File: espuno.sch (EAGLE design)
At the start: 62 parts, among them J1 ARDUINO_R3_SHIELD, T1 FDN340P, U1 ADS1115IDGST, U2 NCP1117ST50T3G, U3 LP2985-33DBVR, U4 FT232R, U5 LMV358IDGKR, U6 MCP73831, U7 TPS61200, X1 POWERSUPPLY_DC21MMX

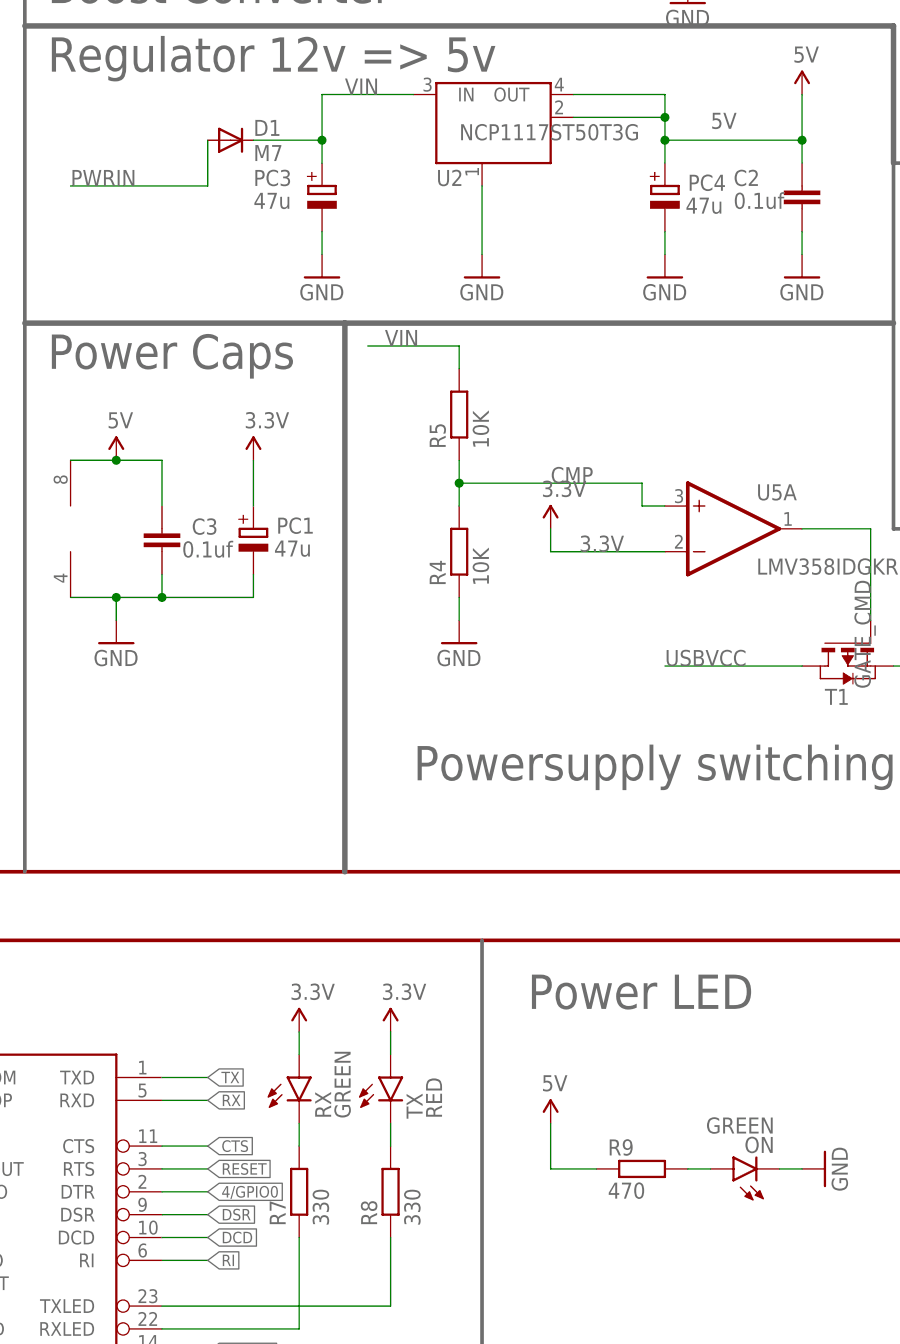
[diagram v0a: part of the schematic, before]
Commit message: Fix bug with TX/RX switched, renumber PC1,PC3,PC4 to be PC1-3 in order of decreasing voltage rail.
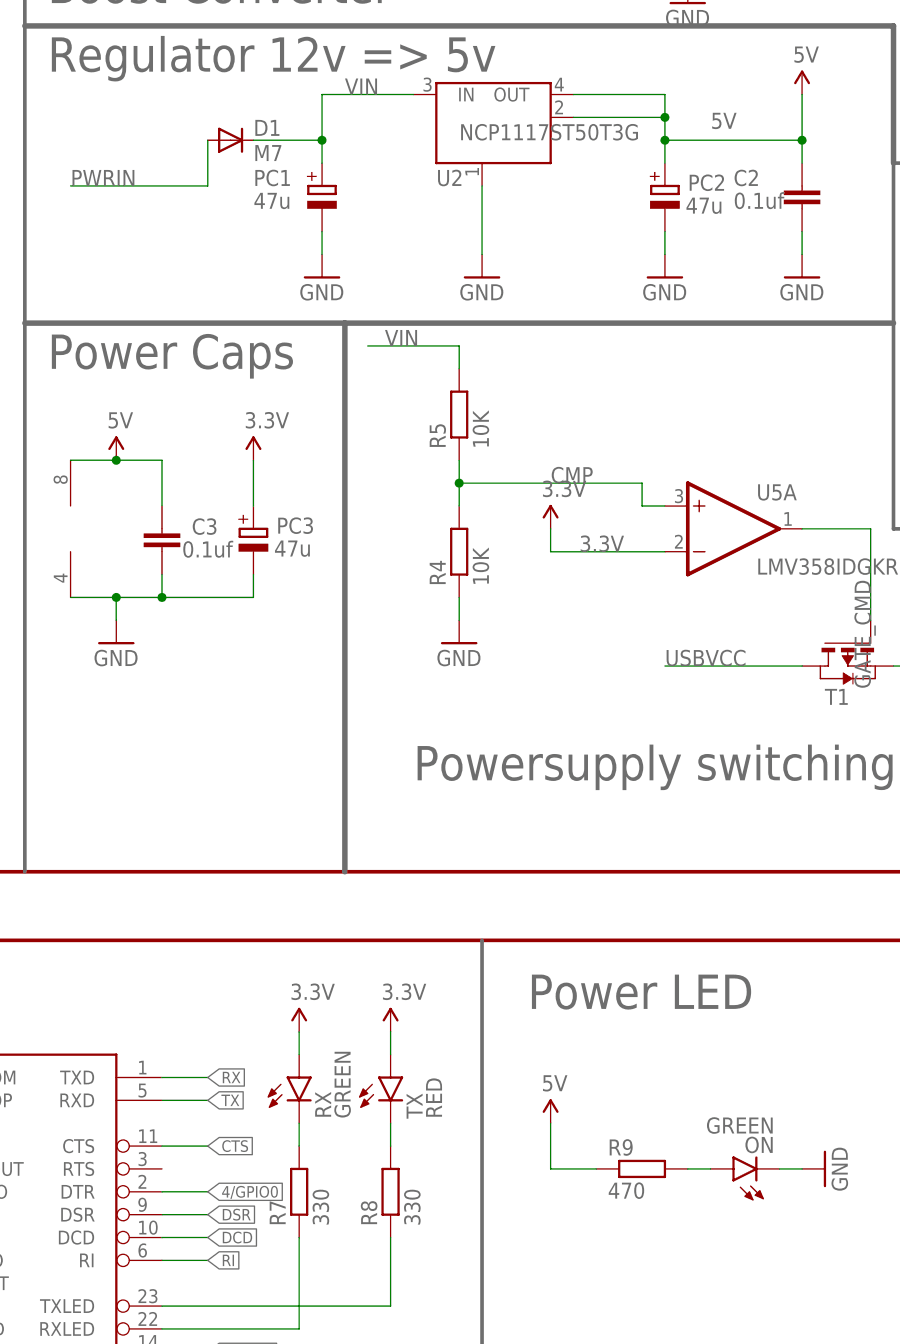
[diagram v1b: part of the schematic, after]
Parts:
- renumbered PC4 to PC2
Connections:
- net 3.3V: now also PC3.+; no longer PC1.+
- net RESET: no longer U4.RTS
- net RX: now also U4.TXD; no longer U4.RXD
- net TX: now also U4.RXD; no longer U4.TXD
- net VIN: now also PC1.+; no longer PC3.+
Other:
- moved on the sheet: PC1, PC3
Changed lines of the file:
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@@
 <?xml version="1.0" encoding="utf-8"?>
 <!DOCTYPE eagle SYSTEM "eagle.dtd">
-<eagle version="7.2.0">
+<eagle version="7.4.0">
 <drawing>
 <settings>
@@
 <part name="JP1" library="SparkFun-Connectors" deviceset="USB" device="-SMD-NS"/>
 <part name="J1" library="SparkFun-Boards" deviceset="ARDUINO_R3_SHIELD" device=""/>
+<part name="PC1" library="rcl" deviceset="CPOL-EU" device="D" value="47u"/>
+<part name="PC2" library="rcl" deviceset="CPOL-EU" device="D" value="47u"/>
 <part name="PC3" library="rcl" deviceset="CPOL-EU" device="D" value="47u"/>
-<part name="PC4" library="rcl" deviceset="CPOL-EU" device="D" value="47u"/>
-<part name="PC1" library="rcl" deviceset="CPOL-EU" device="D" value="47u"/>
 <part name="SUPPLY15" library="SparkFun-Aesthetics" deviceset="3.3V" device=""/>
 <part name="FLASH" library="switch-omron" deviceset="10-XX" device=""/>
@@
 <instance part="JP1" gate="G$1" x="22.86" y="233.68" rot="MR0"/>
 <instance part="J1" gate="G$1" x="40.64" y="287.02"/>
-<instance part="PC3" gate="G$1" x="119.38" y="269.24" smashed="yes">
+<instance part="PC1" gate="G$1" x="119.38" y="269.24" smashed="yes">
 <attribute name="NAME" x="111.76" y="269.24" size="1.778" layer="95"/>
 <attribute name="VALUE" x="111.76" y="266.7" size="1.778" layer="96"/>
 </instance>
-<instance part="PC4" gate="G$1" x="157.48" y="269.24" smashed="yes">
+<instance part="PC2" gate="G$1" x="157.48" y="269.24" smashed="yes">
 <attribute name="NAME" x="160.02" y="268.7066" size="1.778" layer="95"/>
 <attribute name="VALUE" x="159.766" y="266.1666" size="1.778" layer="96"/>
 </instance>
-<instance part="PC1" gate="G$1" x="111.76" y="231.14" smashed="yes">
+<instance part="PC3" gate="G$1" x="111.76" y="231.14" smashed="yes">
 <attribute name="NAME" x="114.3" y="230.6066" size="1.778" layer="95"/>
 <attribute name="VALUE" x="114.046" y="228.0666" size="1.778" layer="96"/>
@@
 <label x="226.06" y="167.64" size="1.778" layer="95"/>
 </segment>
-<segment>
-<wire x1="101.6" y1="160.02" x2="106.68" y2="160.02" width="0.1524" layer="91"/>
-<pinref part="U4" gate="G$1" pin="RTS"/>
-<label x="106.68" y="160.02" size="1.27" layer="95" xref="yes"/>
-</segment>
 </net>
 <net name="3.3V" class="0">
@@
 <segment>
 <pinref part="SUPPLY15" gate="G$1" pin="3.3V"/>
-<pinref part="PC1" gate="G$1" pin="+"/>
+<pinref part="PC3" gate="G$1" pin="+"/>
 <wire x1="111.76" y1="238.76" x2="111.76" y2="233.68" width="0.1524" layer="91"/>
 </segment>
@@
 <wire x1="157.48" y1="264.16" x2="157.48" y2="261.62" width="0.1524" layer="91"/>
 <pinref part="GND10" gate="1" pin="GND"/>
-<pinref part="PC4" gate="G$1" pin="-"/>
+<pinref part="PC2" gate="G$1" pin="-"/>
 </segment>
 <segment>
 <wire x1="119.38" y1="261.62" x2="119.38" y2="264.16" width="0.1524" layer="91"/>
 <pinref part="GND9" gate="1" pin="GND"/>
-<pinref part="PC3" gate="G$1" pin="-"/>
+<pinref part="PC1" gate="G$1" pin="-"/>
 </segment>
 <segment>
@@
 <pinref part="U5" gate="P" pin="V-"/>
 <wire x1="111.76" y1="226.06" x2="111.76" y2="223.52" width="0.1524" layer="91"/>
-<pinref part="PC1" gate="G$1" pin="-"/>
+<pinref part="PC3" gate="G$1" pin="-"/>
 <wire x1="111.76" y1="223.52" x2="101.6" y2="223.52" width="0.1524" layer="91"/>
 <junction x="101.6" y="223.52"/>
@@
 </segment>
 <segment>
+<wire x1="53.34" y1="304.8" x2="66.04" y2="304.8" width="0.1524" layer="91"/>
+<pinref part="J1" gate="G$1" pin="RX"/>
+<label x="55.88" y="304.8" size="1.778" layer="95"/>
+</segment>
+<segment>
+<wire x1="101.6" y1="170.18" x2="106.68" y2="170.18" width="0.1524" layer="91"/>
+<pinref part="U4" gate="G$1" pin="TXD"/>
+<label x="106.68" y="170.18" size="1.27" layer="95" xref="yes"/>
+</segment>
+</net>
+<net name="TX" class="0">
+<segment>
+<wire x1="76.2" y1="360.68" x2="55.88" y2="360.68" width="0.1524" layer="91"/>
+<label x="63.5" y="360.68" size="1.778" layer="95"/>
+<pinref part="MDL1" gate="G$1" pin="TXD"/>
+</segment>
+<segment>
+<pinref part="J1" gate="G$1" pin="TX"/>
+<wire x1="53.34" y1="302.26" x2="66.04" y2="302.26" width="0.1524" layer="91"/>
+<label x="55.88" y="302.26" size="1.778" layer="95"/>
+</segment>
+<segment>
 <wire x1="101.6" y1="167.64" x2="106.68" y2="167.64" width="0.1524" layer="91"/>
 <pinref part="U4" gate="G$1" pin="RXD"/>
 <label x="106.68" y="167.64" size="1.27" layer="95" xref="yes"/>
-</segment>
-<segment>
-<wire x1="53.34" y1="304.8" x2="66.04" y2="304.8" width="0.1524" layer="91"/>
-<pinref part="J1" gate="G$1" pin="RX"/>
-<label x="55.88" y="304.8" size="1.778" layer="95"/>
-</segment>
-</net>
-<net name="TX" class="0">
-<segment>
-<wire x1="76.2" y1="360.68" x2="55.88" y2="360.68" width="0.1524" layer="91"/>
-<label x="63.5" y="360.68" size="1.778" layer="95"/>
-<pinref part="MDL1" gate="G$1" pin="TXD"/>
-</segment>
-<segment>
-<wire x1="101.6" y1="170.18" x2="106.68" y2="170.18" width="0.1524" layer="91"/>
-<pinref part="U4" gate="G$1" pin="TXD"/>
-<label x="106.68" y="170.18" size="1.27" layer="95" xref="yes"/>
-</segment>
-<segment>
-<pinref part="J1" gate="G$1" pin="TX"/>
-<wire x1="53.34" y1="302.26" x2="66.04" y2="302.26" width="0.1524" layer="91"/>
-<label x="55.88" y="302.26" size="1.778" layer="95"/>
 </segment>
 </net>
@@
 <pinref part="C2" gate="G$1" pin="2"/>
 <junction x="172.72" y="274.32"/>
-<pinref part="PC4" gate="G$1" pin="+"/>
+<pinref part="PC2" gate="G$1" pin="+"/>
 </segment>
 <segment>
@@
 <pinref part="U2" gate="G$1" pin="IN"/>
 <pinref part="D1" gate="G$1" pin="C"/>
-<pinref part="PC3" gate="G$1" pin="+"/>
-</segment>
-<segment>
+<pinref part="PC1" gate="G$1" pin="+"/>
+</segment>
+<segment>

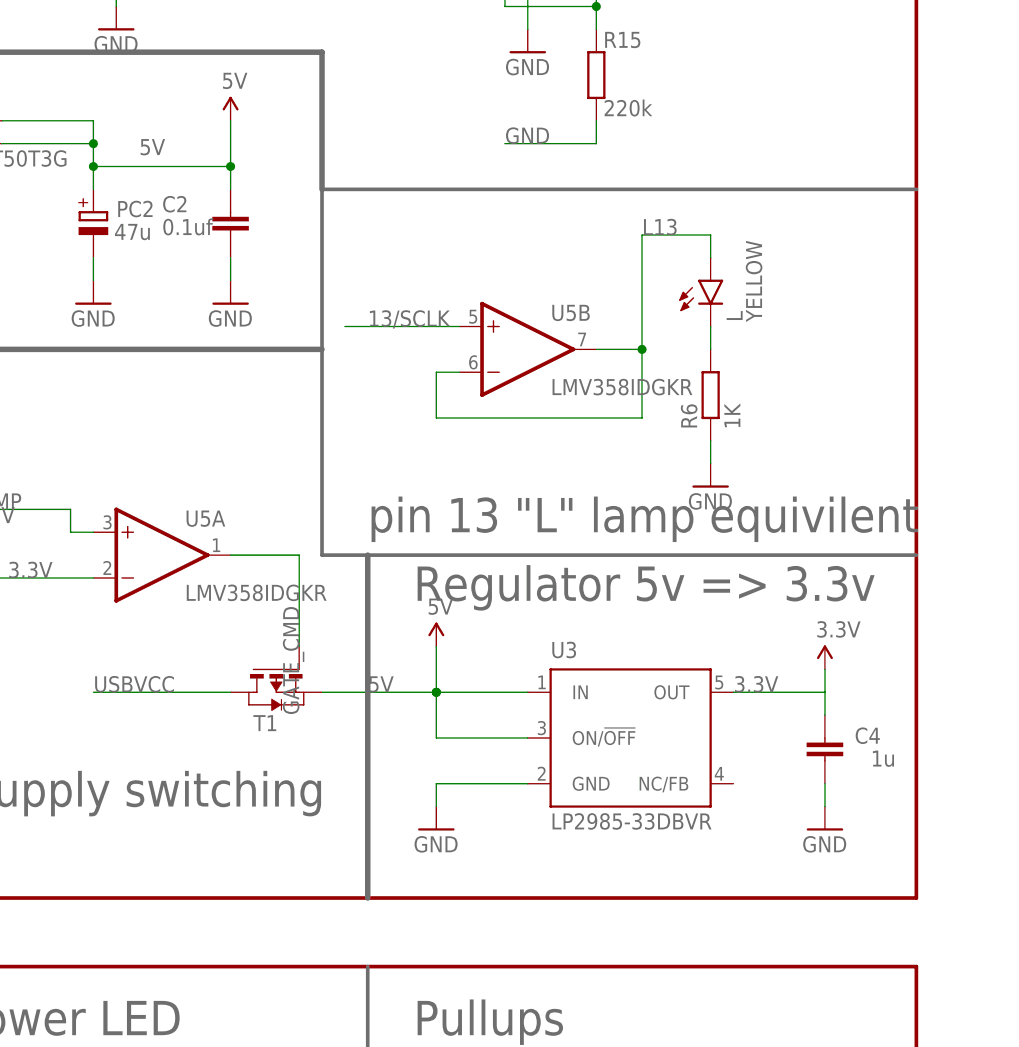
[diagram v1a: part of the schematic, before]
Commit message: Change puny 3.3v regulator for a 800mA-1A regulator. Rearrangements to make space, remove redundent capacitor
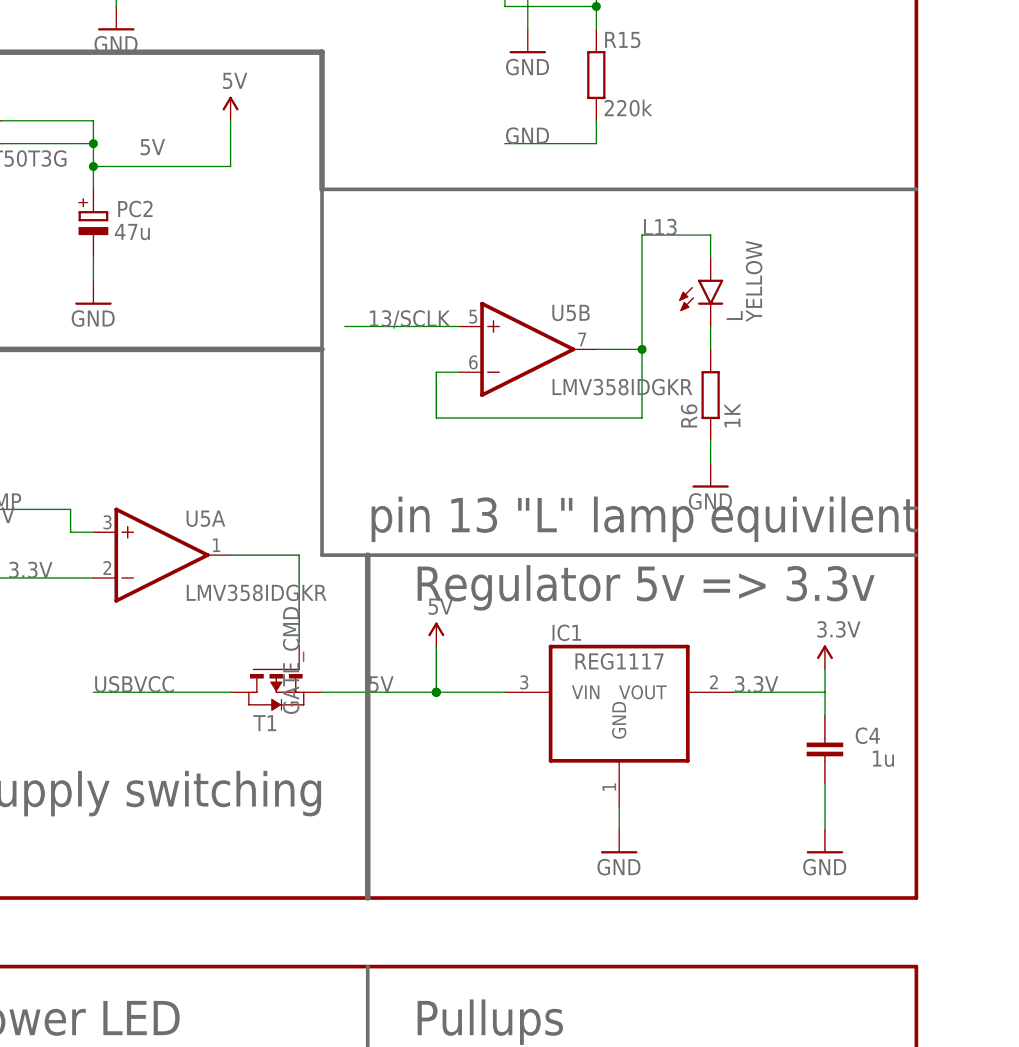
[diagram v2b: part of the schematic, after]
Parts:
- removed C2: 0.1uf, rcl:C-EUC1206K
- removed U3: LP2985-33DBVR, SmartPrj:LP2985-XXDBVR33
- added IC1: REG1117, burr-brown:REG1117
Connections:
- net 3.3V: now also IC1.VOUT; no longer U3.OUT
- net 5V: now also IC1.VIN; no longer C2.2, U3.IN, U3.ON/!OFF
- net GND: now also IC1.GND; no longer C2.1, U3.GND
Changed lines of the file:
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@@
 <part name="R3" library="rcl" deviceset="R-EU_" device="M1206" value="10K"/>
 <part name="U$6" library="microbuilder" deviceset="GND" device=""/>
-<part name="C2" library="rcl" deviceset="C-EU" device="C1206K" value="0.1uf"/>
-<part name="GND7" library="supply1" deviceset="GND" device=""/>
 <part name="GND9" library="supply1" deviceset="GND" device=""/>
 <part name="GND10" library="supply1" deviceset="GND" device=""/>
@@
 <part name="C4" library="rcl" deviceset="C-EU" device="C1206K" value="1u"/>
 <part name="U5" library="linear" deviceset="LMV358?*" device="MM" technology="X" value="LMV358IDGKR"/>
-<part name="U3" library="SmartPrj" deviceset="LP2985-XXDBVR" device="" technology="33" value="LP2985-33DBVR"/>
 <part name="R4" library="rcl" deviceset="R-EU_" device="M1206" value="10K"/>
 <part name="R5" library="rcl" deviceset="R-EU_" device="M1206" value="10K"/>
@@
 <part name="R20" library="SparkFun-Resistors" deviceset="RESISTOR" device="1206" value="10k"/>
 <part name="R21" library="SparkFun-Resistors" deviceset="RESISTOR" device="1206" value="10k"/>
+<part name="IC1" library="burr-brown" deviceset="REG1117" device=""/>
 </parts>
 <sheets>
@@
 <instance part="R3" gate="G$1" x="73.66" y="68.58" rot="R270"/>
 <instance part="U$6" gate="G$1" x="73.66" y="58.42"/>
-<instance part="C2" gate="G$1" x="172.72" y="266.7" smashed="yes" rot="R180">
-<attribute name="NAME" x="165.1" y="269.24" size="1.778" layer="95"/>
-<attribute name="VALUE" x="165.1" y="266.7" size="1.778" layer="96"/>
-</instance>
-<instance part="GND7" gate="1" x="172.72" y="259.08"/>
 <instance part="GND9" gate="1" x="119.38" y="259.08"/>
 <instance part="GND10" gate="1" x="157.48" y="259.08"/>
@@
 <attribute name="VALUE" x="109.474" y="227.965" size="1.778" layer="96" rot="MR0"/>
 </instance>
-<instance part="GND21" gate="1" x="238.76" y="200.66"/>
-<instance part="GND4" gate="1" x="195.58" y="200.66"/>
+<instance part="GND21" gate="1" x="238.76" y="198.12"/>
+<instance part="GND4" gate="1" x="215.9" y="198.12"/>
 <instance part="C4" gate="G$1" x="238.76" y="208.28" smashed="yes" rot="MR180">
 <attribute name="NAME" x="244.983" y="210.185" size="1.778" layer="95" rot="MR0"/>
@@
 <instance part="U5" gate="B" x="205.74" y="254"/>
 <instance part="U5" gate="P" x="91.44" y="231.14"/>
-<instance part="U3" gate="G$1" x="215.9" y="210.82"/>
 <instance part="R4" gate="G$1" x="134.62" y="228.6" rot="R90"/>
 <instance part="R5" gate="G$1" x="134.62" y="243.84" rot="R90"/>
@@
 <instance part="R20" gate="G$1" x="218.44" y="152.4"/>
 <instance part="R21" gate="G$1" x="218.44" y="129.54"/>
+<instance part="IC1" gate="G$1" x="215.9" y="215.9"/>
 </instances>
 <busses>
@@
 <label x="228.6" y="215.9" size="1.778" layer="95"/>
 <pinref part="C4" gate="G$1" pin="2"/>
-<pinref part="U3" gate="G$1" pin="OUT"/>
 <pinref part="SUPPLY12" gate="G$1" pin="3.3V"/>
 <wire x1="238.76" y1="218.44" x2="238.76" y2="215.9" width="0.1524" layer="91"/>
+<pinref part="IC1" gate="G$1" pin="VOUT"/>
 </segment>
 <segment>
@@
 </segment>
 <segment>
-<wire x1="172.72" y1="264.16" x2="172.72" y2="261.62" width="0.1524" layer="91"/>
-<pinref part="C2" gate="G$1" pin="1"/>
-<pinref part="GND7" gate="1" pin="GND"/>
-</segment>
-<segment>
 <wire x1="157.48" y1="264.16" x2="157.48" y2="261.62" width="0.1524" layer="91"/>
 <pinref part="GND10" gate="1" pin="GND"/>
@@
 </segment>
 <segment>
-<wire x1="238.76" y1="203.2" x2="238.76" y2="205.74" width="0.1524" layer="91"/>
+<wire x1="238.76" y1="200.66" x2="238.76" y2="205.74" width="0.1524" layer="91"/>
 <pinref part="GND21" gate="1" pin="GND"/>
 <pinref part="C4" gate="G$1" pin="1"/>
 </segment>
 <segment>
-<wire x1="205.74" y1="205.74" x2="195.58" y2="205.74" width="0.1524" layer="91"/>
-<wire x1="195.58" y1="205.74" x2="195.58" y2="203.2" width="0.1524" layer="91"/>
+<wire x1="215.9" y1="203.2" x2="215.9" y2="200.66" width="0.1524" layer="91"/>
 <pinref part="GND4" gate="1" pin="GND"/>
-<pinref part="U3" gate="G$1" pin="GND"/>
+<pinref part="IC1" gate="G$1" pin="GND"/>
 </segment>
 <segment>
@@
 <wire x1="157.48" y1="276.86" x2="157.48" y2="274.32" width="0.1524" layer="91"/>
 <wire x1="157.48" y1="274.32" x2="172.72" y2="274.32" width="0.1524" layer="91"/>
-<wire x1="172.72" y1="274.32" x2="172.72" y2="271.78" width="0.1524" layer="91"/>
 <junction x="157.48" y="276.86"/>
 <junction x="157.48" y="274.32"/>
@@
 <pinref part="U2" gate="G$1" pin="OUT@1"/>
 <pinref part="U2" gate="G$1" pin="OUT"/>
-<pinref part="C2" gate="G$1" pin="2"/>
-<junction x="172.72" y="274.32"/>
 <pinref part="PC2" gate="G$1" pin="+"/>
 </segment>
@@
 </segment>
 <segment>
-<wire x1="195.58" y1="215.9" x2="205.74" y2="215.9" width="0.1524" layer="91"/>
-<wire x1="205.74" y1="210.82" x2="195.58" y2="210.82" width="0.1524" layer="91"/>
-<wire x1="195.58" y1="210.82" x2="195.58" y2="215.9" width="0.1524" layer="91"/>
+<wire x1="195.58" y1="215.9" x2="203.2" y2="215.9" width="0.1524" layer="91"/>
 <wire x1="182.88" y1="215.9" x2="195.58" y2="215.9" width="0.1524" layer="91"/>
 <junction x="195.58" y="215.9"/>
 <label x="187.96" y="215.9" size="1.778" layer="95"/>
 <pinref part="T1" gate="A" pin="S"/>
-<pinref part="U3" gate="G$1" pin="IN"/>
-<pinref part="U3" gate="G$1" pin="ON/!OFF"/>
 <pinref part="SUPPLY7" gate="G$1" pin="5V"/>
 <wire x1="195.58" y1="220.98" x2="195.58" y2="215.9" width="0.1524" layer="91"/>
 <junction x="195.58" y="215.9"/>
-</segment>
-<segment>
+<pinref part="IC1" gate="G$1" pin="VIN"/>
+</segment>
+<segment>
